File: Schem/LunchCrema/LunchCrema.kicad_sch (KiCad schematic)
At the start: 0 parts

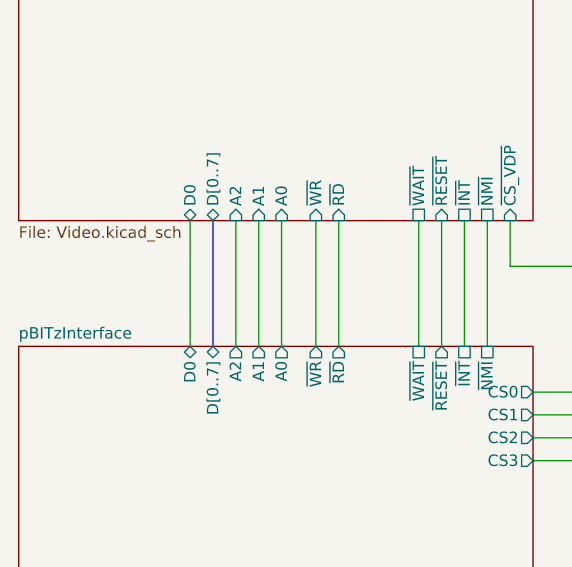
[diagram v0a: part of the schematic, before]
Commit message: Added wait state generator to LaunchCrema
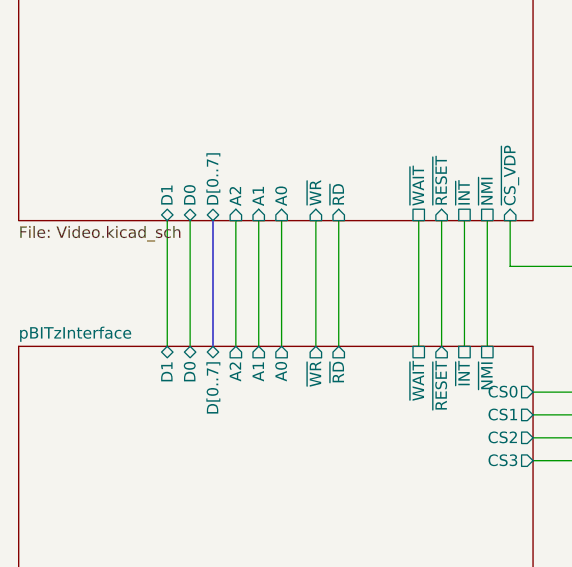
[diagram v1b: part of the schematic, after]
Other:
- sheet Video ports: added D1; removed none
- sheet pBITzInterface ports: added D1; removed none
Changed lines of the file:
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@@
+	(wire
+		(pts
+			(xy 50.8 60.96) (xy 50.8 74.93)
+		)
+		(stroke
+			(width 0)
+			(type default)
+		)
+	)
 	(wire
 		(pts
@@
 			)
 		)
+		(pin "D1" bidirectional
+			(at 50.8 60.96 270)
+			(effects
+				(font
+					(size 1.27 1.27)
+				)
+				(justify left)
+			)
+		)
 		(instances
 			(project "LunchCrema"
@@
 			(effects
 				(font
+					(size 1.27 1.27)
+				)
+				(justify right)
+			)
+		)
+		(pin "D1" bidirectional
+			(at 50.8 74.93 90)
+			(effects
+				(font
